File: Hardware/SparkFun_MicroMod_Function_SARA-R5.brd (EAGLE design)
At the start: 37.5 x 65 mm, 129 parts, among them J1 MICROMOD_FUNCTION_STANDARD, J2 U.FL, J4 U.FL, J9 NANO_SIM, Q2 310mA/60V/1.6Ω, Q3 310mA/60V/1.6Ω, Q5 310mA/60V/1.6Ω, Q6 310mA/60V/1.6Ω, U1 SARA-R510M8S, U11 74HC1G04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

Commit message: SIM clock routing to a "Y" to avoid 90 degree.
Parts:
- moved U$5 5.72 mm to (25.2, 4.45)
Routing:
- net GND: track 40.9 -> 43.7 mm
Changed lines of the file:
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@@
 <element name="U$18" library="output" package="NANO0" value="" x="27.983184375" y="24.718340625" smashed="yes"/>
 <element name="U$126" library="output" package="SIM0" value="" x="31.295340625" y="24.708175" smashed="yes"/>
-<element name="U$5" library="HPG_Solution" package="ON0" value="" x="25.3492" y="10.1616" smashed="yes"/>
+<element name="U$5" library="HPG_Solution" package="ON0" value="" x="25.2222" y="4.4466" smashed="yes"/>
 <element name="U$12" library="SparkFun-MicroMod" package="MICROMOD_MI_LOGO_1" value="" x="10.033" y="32.92" smashed="yes"/>
 <element name="J2" library="SparkFun-Connectors" package="U.FL" value="U.FL" x="31.64" y="60.96" smashed="yes" rot="R270">
@@
 <via x="34.012203125" y="8.275315625" extent="1-16" drill="0.3048" diameter="0.6096"/>
 <via x="32.3332625" y="6.2738" extent="1-16" drill="0.3048" diameter="0.6096"/>
-<via x="23.89538125" y="16.96974375" extent="1-16" drill="0.3048" diameter="0.6096"/>
+<via x="23.7480625" y="16.90370625" extent="1-16" drill="0.3048" diameter="0.6096"/>
 <via x="23.791240625" y="13.741403125" extent="1-16" drill="0.3048" diameter="0.6096"/>
 <via x="36.808740625" y="32.859978125" extent="1-16" drill="0.3048" diameter="0.6096"/>
@@
 <wire x1="30.286959375" y1="9.780440625" x2="30.286959375" y2="10.382303125" width="0.254" layer="1"/>
 <via x="26.6055625" y="56.30418125" extent="1-16" drill="0.3048" diameter="0.6096"/>
+<wire x1="19.1769625" y1="17.75968125" x2="19.9389625" y2="16.99768125" width="0.254" layer="1"/>
+<wire x1="19.9389625" y1="16.99768125" x2="21.650959375" y2="16.99768125" width="0.254" layer="1"/>
 </signal>
 <signal name="EN">
@@
 <contactref element="J9" pad="C3"/>
 <wire x1="22.691" y1="13.082" x2="24.11068125" y2="13.082" width="0.254" layer="1"/>
-<wire x1="24.884384375" y1="13.855703125" x2="24.884384375" y2="16.7919375" width="0.254" layer="1"/>
+<wire x1="24.884384375" y1="13.855703125" x2="24.884384375" y2="16.534496875" width="0.254" layer="1"/>
 <wire x1="24.11068125" y1="13.082" x2="24.884384375" y2="13.855703125" width="0.254" layer="1"/>
 <contactref element="U1" pad="38"/>
@@
 <wire x1="13.55" y1="37.476059375" x2="21.55951875" y2="29.466540625" width="0.254" layer="1"/>
 <wire x1="21.55951875" y1="29.466540625" x2="25.861340625" y2="29.466540625" width="0.254" layer="1"/>
-<wire x1="20.8769625" y1="17.75968125" x2="21.6535" y2="17.75968125" width="0.254" layer="1"/>
-<wire x1="21.6535" y1="17.75968125" x2="21.8795625" y2="17.53361875" width="0.254" layer="1"/>
-<wire x1="21.8795625" y1="17.53361875" x2="24.151959375" y2="17.53361875" width="0.254" layer="1"/>
-<wire x1="24.151959375" y1="17.523459375" x2="24.1528625" y2="17.523459375" width="0.254" layer="1"/>
-<wire x1="24.884384375" y1="16.7919375" x2="24.1528625" y2="17.523459375" width="0.254" layer="1"/>
-<wire x1="24.151959375" y1="17.523459375" x2="24.151959375" y2="17.53361875" width="0.254" layer="1"/>
-<wire x1="24.151959375" y1="17.53361875" x2="24.151959375" y2="21.374103125" width="0.254" layer="1"/>
-<wire x1="24.9571375" y1="22.17928125" x2="24.151959375" y2="21.374103125" width="0.254" layer="1"/>
+<wire x1="24.884384375" y1="16.534496875" x2="23.8624" y2="17.55648125" width="0.254" layer="1"/>
+<wire x1="24.9571375" y1="22.17928125" x2="24.234140625" y2="21.456284375" width="0.254" layer="1"/>
 <wire x1="26.96878125" y1="22.7346" x2="26.4134625" y2="22.17928125" width="0.254" layer="1"/>
 <wire x1="26.4134625" y1="22.17928125" x2="24.9571375" y2="22.17928125" width="0.254" layer="1"/>
+<wire x1="24.234140625" y1="17.928221875" x2="23.8624" y2="17.55648125" width="0.254" layer="1"/>
+<wire x1="24.234140625" y1="21.456284375" x2="24.234140625" y2="17.928221875" width="0.254" layer="1"/>
+<wire x1="20.8769625" y1="17.75968125" x2="21.76018125" y2="17.75968125" width="0.254" layer="1"/>
+<wire x1="21.76018125" y1="17.75968125" x2="21.9837" y2="17.5361625" width="0.254" layer="1"/>
+<wire x1="21.9837" y1="17.5361625" x2="23.84208125" y2="17.5361625" width="0.254" layer="1"/>
+<wire x1="23.84208125" y1="17.5361625" x2="23.8624" y2="17.55648125" width="0.254" layer="1"/>
 </signal>
 <signal name="SIM_RST">

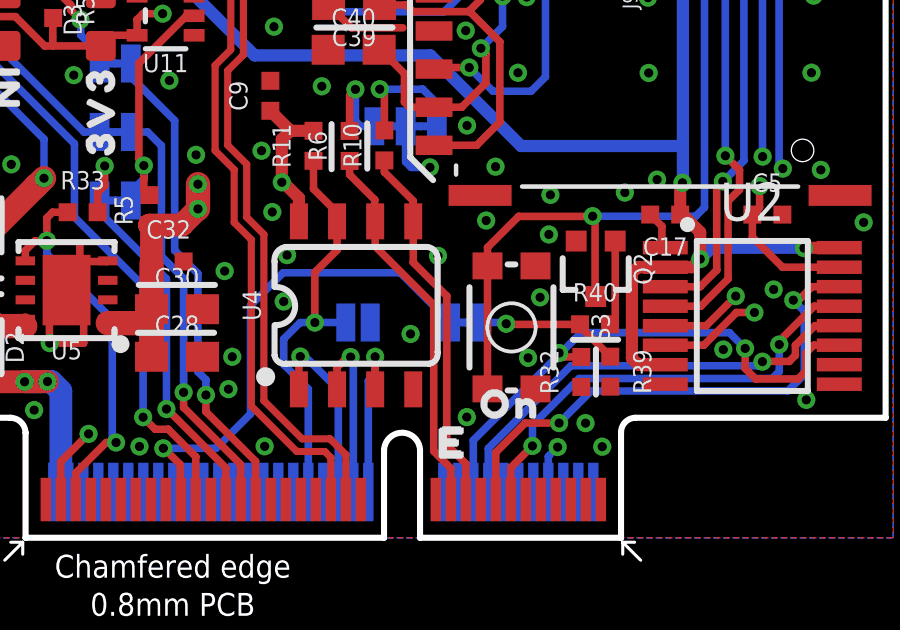
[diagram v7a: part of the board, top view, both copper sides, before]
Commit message: Moved LTE "ON" button north away from the M.2 conn
-note, moved the silk label to the south side of the button to allow this shift.
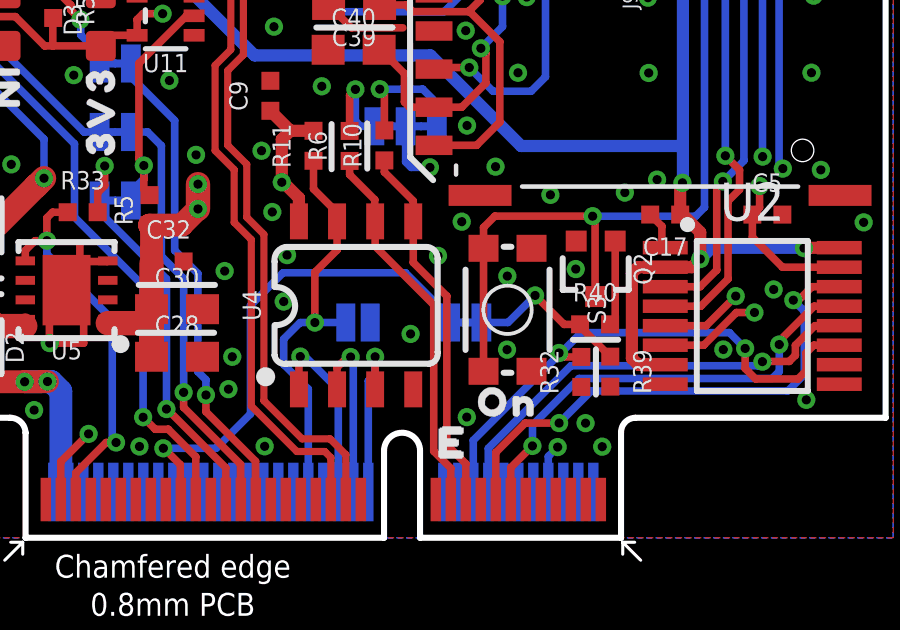
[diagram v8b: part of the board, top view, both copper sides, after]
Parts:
- moved S3 0.60 mm to (25.1, 7.60)
- moved U$5 0.11 mm to (25.1, 4.52)
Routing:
- net LTE_PWR_ON: track 4.81 -> 5.56 mm
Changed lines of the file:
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@@
 <drawing>
 <settings>
-<setting alwaysvectorfont="no"/>
+<setting alwaysvectorfont="yes"/>
 <setting verticaltext="up"/>
 </settings>
@@
 <attribute name="VALUE" x="34.6599" y="36.375340625" size="0.6096" layer="27" font="vector" ratio="20" align="top-center"/>
 </element>
-<element name="S3" library="SparkFun-Switches" package="TACTILE_SWITCH_SMD_4.6X2.8MM" value="PWR_ON" x="25.273" y="7.012" smashed="yes" rot="R270">
-<attribute name="NAME" x="27.94" y="7.012" size="0.6096" layer="25" font="vector" ratio="20" rot="R270" align="bottom-center"/>
-<attribute name="PROD_ID" value="SWCH-15606" x="-224.917" y="134.012" size="1.778" layer="27" font="vector" ratio="15" rot="R270" display="off"/>
-<attribute name="VALUE" x="22.606" y="7.012" size="0.6096" layer="27" font="vector" ratio="20" rot="R270" align="top-center"/>
+<element name="S3" library="SparkFun-Switches" package="TACTILE_SWITCH_SMD_4.6X2.8MM" value="PWR_ON" x="25.140921875" y="7.598740625" smashed="yes" rot="R270">
+<attribute name="NAME" x="27.807921875" y="7.598740625" size="0.6096" layer="25" font="vector" ratio="20" rot="R270" align="bottom-center"/>
+<attribute name="PROD_ID" value="SWCH-15606" x="-225.049078125" y="134.598740625" size="1.778" layer="27" font="vector" ratio="15" rot="R270" display="off"/>
+<attribute name="VALUE" x="22.473921875" y="7.598740625" size="0.6096" layer="27" font="vector" ratio="20" rot="R270" align="top-center"/>
 </element>
 <element name="R1" library="SparkFun-Resistors" package="0402-TIGHT" value="100k" x="22.5425" y="55.2085" smashed="yes">
@@
 <element name="U$18" library="output" package="NANO0" value="" x="27.983184375" y="24.718340625" smashed="yes"/>
 <element name="U$126" library="output" package="SIM0" value="" x="31.295340625" y="24.708175" smashed="yes"/>
-<element name="U$5" library="HPG_Solution" package="ON0" value="" x="25.2222" y="4.4466" smashed="yes"/>
+<element name="U$5" library="HPG_Solution" package="ON0" value="" x="25.13838125" y="4.51518125" smashed="yes"/>
 <element name="U$12" library="SparkFun-MicroMod" package="MICROMOD_MI_LOGO_1" value="" x="10.033" y="32.92" smashed="yes"/>
 <element name="J2" library="SparkFun-Connectors" package="U.FL" value="U.FL" x="31.64" y="60.96" smashed="yes" rot="R270">
@@
 <via x="4.6752" y="21.06168125" extent="1-16" drill="0.3048" diameter="0.6096"/>
 <via x="10.187" y="24.13" extent="1-16" drill="0.3048" diameter="0.6096"/>
-<via x="26.2271" y="8.0137" extent="1-16" drill="0.3048" diameter="0.6096"/>
+<via x="25.1349" y="8.7223625" extent="1-16" drill="0.3048" diameter="0.6096"/>
 <via x="19.9761625" y="18.826478125" extent="1-16" drill="0.3048" diameter="0.6096"/>
 <via x="19.9507625" y="20.322540625" extent="1-16" drill="0.3048" diameter="0.6096"/>
@@
 <via x="23.557559375" y="18.785840625" extent="1-16" drill="0.3048" diameter="0.6096"/>
 <contactref element="J9" pad="C5"/>
-<via x="24.429721875" y="10.574021875" extent="1-16" drill="0.3048" diameter="0.6096"/>
-<via x="25.82578125" y="5.996940625" extent="1-16" drill="0.3048" diameter="0.6096"/>
-<via x="26.5192" y="10.1092" extent="1-16" drill="0.3048" diameter="0.6096"/>
+<via x="23.61438125" y="10.535921875" extent="1-16" drill="0.3048" diameter="0.6096"/>
+<via x="25.12474375" y="6.2712625" extent="1-16" drill="0.3048" diameter="0.6096"/>
+<via x="27.41581875" y="8.95604375" extent="1-16" drill="0.3048" diameter="0.6096"/>
 <via x="33.49911875" y="26.1137375" extent="1-16" drill="0.3048" diameter="0.6096"/>
 <via x="16.940859375" y="12.900659375" extent="1-16" drill="0.3048" diameter="0.6096"/>
@@
 <contactref element="S3" pad="2"/>
 <contactref element="S3" pad="1"/>
-<wire x1="24.473" y1="9.062" x2="24.473" y2="4.962" width="0.254" layer="1"/>
+<wire x1="24.340921875" y1="9.648740625" x2="24.340921875" y2="5.548740625" width="0.254" layer="1"/>
 <via x="27.9776" y="10.7188" extent="1-16" drill="0.3048" diameter="0.6096"/>
 <wire x1="27.9776" y1="10.7188" x2="31.41168125" y2="10.7188" width="0.254" layer="16"/>
-<wire x1="24.473" y1="9.062" x2="24.473" y2="9.674959375" width="0.254" layer="1"/>
-<wire x1="27.9776" y1="10.7188" x2="27.972" y2="10.7132" width="0.254" layer="1"/>
-<wire x1="27.972" y1="10.7132" x2="25.511240625" y2="10.7132" width="0.254" layer="1"/>
-<wire x1="24.473" y1="9.674959375" x2="25.511240625" y2="10.7132" width="0.254" layer="1"/>
+<wire x1="27.9776" y1="10.7188" x2="27.97558125" y2="10.72081875" width="0.254" layer="1"/>
+<wire x1="27.97558125" y1="10.72081875" x2="24.718759375" y2="10.72081875" width="0.254" layer="1"/>
+<wire x1="24.718759375" y1="10.72081875" x2="24.340921875" y2="10.34298125" width="0.254" layer="1"/>
+<wire x1="24.340921875" y1="9.648740625" x2="24.340921875" y2="10.34298125" width="0.254" layer="1"/>
 <wire x1="28.0797" y1="8.0396" x2="28.0591" y2="8.0602" width="0.254" layer="1"/>
 <wire x1="28.0591" y1="8.0602" x2="28.0591" y2="10.6373" width="0.254" layer="1"/>
@@
 <contactref element="R40" pad="1"/>
 <contactref element="R39" pad="1"/>
-<via x="25.0968" y="7.132321875" extent="1-16" drill="0.3048" diameter="0.6096"/>
+<via x="26.059459375" y="8.077203125" extent="1-16" drill="0.3048" diameter="0.6096"/>
 <wire x1="27.55938125" y1="7.11548125" x2="27.5559" y2="7.112" width="0.254" layer="1"/>
-<wire x1="27.5559" y1="7.112" x2="25.117121875" y2="7.112" width="0.254" layer="1"/>
-<wire x1="25.0968" y1="7.132321875" x2="25.117121875" y2="7.112" width="0.254" layer="1"/>
+<wire x1="27.5559" y1="7.112" x2="27.0246625" y2="7.112" width="0.254" layer="1"/>
+<wire x1="26.059459375" y1="8.077203125" x2="27.0246625" y2="7.112" width="0.254" layer="1"/>
 <wire x1="27.577159375" y1="7.097703125" x2="27.55938125" y2="7.11548125" width="0.254" layer="1"/>
 <wire x1="28.565778125" y1="6.037203125" x2="27.577159375" y2="7.025821875" width="0.254" layer="1"/>
 <wire x1="27.577159375" y1="7.025821875" x2="27.577159375" y2="7.097703125" width="0.254" layer="1"/>
 <contactref element="LTE_PWR_ON" pad="1"/>
-<wire x1="25.0968" y1="7.132321875" x2="25.053621875" y2="7.1755" width="0.254" layer="16"/>
-<wire x1="25.053621875" y1="7.1755" x2="24.2697" y2="7.1755" width="0.254" layer="16"/>
+<wire x1="26.059459375" y1="8.077203125" x2="25.15775625" y2="7.1755" width="0.254" layer="16"/>
+<wire x1="25.15775625" y1="7.1755" x2="24.2697" y2="7.1755" width="0.254" layer="16"/>
 </signal>
 <signal name="LTE_!RESET!">
@@
 <signal name="N$3">
 <contactref element="LTE_PWR_ON" pad="2"/>
-<wire x1="23.2283" y1="7.1755" x2="21.572221875" y2="8.831578125" width="0.254" layer="16"/>
+<wire x1="23.2283" y1="7.1755" x2="23.2283" y2="7.3431375" width="0.254" layer="16"/>
+<wire x1="23.2283" y1="7.3431375" x2="21.739859375" y2="8.831578125" width="0.254" layer="16"/>
 <wire x1="17.656809375" y1="8.831578125" x2="16.5735" y2="7.74826875" width="0.254" layer="16"/>
 <wire x1="16.5735" y1="7.74826875" x2="16.5735" y2="4.1275" width="0.254" layer="16"/>
@@
 <wire x1="15.427959375" y1="2.981959375" x2="13.667740625" y2="2.981959375" width="0.254" layer="16"/>
 <via x="13.667740625" y="2.981959375" extent="1-16" drill="0.3048" diameter="0.6096"/>
-<wire x1="21.572221875" y1="8.831578125" x2="17.656809375" y2="8.831578125" width="0.254" layer="16"/>
+<wire x1="21.739859375" y1="8.831578125" x2="17.656809375" y2="8.831578125" width="0.254" layer="16"/>
 <contactref element="J1" pad="57"/>
 <wire x1="14.25" y1="1.275" x2="14.2335" y2="1.2915" width="0.254" layer="1"/>
